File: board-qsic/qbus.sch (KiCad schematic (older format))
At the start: 0 parts

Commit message: Reworked board from template.  Changed schematic to let me use the bus drivers and level converters more efficiently so to get all the signals.
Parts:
- added C501, C502: 100nF, Capacitor_SMD:C_0603_1608Metric, symbol Device:C
- added R501, R502: 4.7k, Resistor_SMD:R_0603_1608Metric, symbol Device:R
- added R503: 2.4k, Resistor_SMD:R_0603_1608Metric, symbol Device:R
- added U101: XC7A75T-CSG324, Package_BGA:BGA-324_15.0x15.0mm_Layout18x18_P0.8mm_Ball0.5mm_Pad0.4mm_NSMD, symbol FPGA_Xilinx_Artix7:XC7A75T-CSG324
- added U501: MT25Q-so8, Package_DFN_QFN:DFN-8-1EP_6x5mm_P1.27mm_EP4x4mm, symbol myLib:MT25Q-mlp8
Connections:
- new net: R503.2, U101.L13 (IO_L6P_T0_FCS_B_14), U501.1 (~S)
- new net: U101.K18 (IO_L1N_T0_D01_DIN_14), U501.2 (DQ1)
- new net: R501.2, U101.L14 (IO_L2P_T0_D02_14), U501.3 (~W~/DQ2)
- new net: U101.K17 (IO_L1P_T0_D00_MOSI_14), U501.5 (DQ0)
- new net: R502.2, U101.M14 (IO_L2N_T0_D03_14), U501.7 (~HOLD~/DQ3)
- new net 3V3: C501.1, C502.1, R501.1, R502.1, R503.1, U101.L17 (VCCO_14), U101.N13 (VCCO_14), U101.P16 (VCCO_14), U101.T12 (VCCO_14), U101.U15 (VCCO_14), U101.V18 (VCCO_14), U501.8 (Vcc)
- new net CCLK: U501.6 (C)
- new net GND: C501.2, C502.2, U501.4 (Vss), U501.9 (EP)

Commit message: Design of prototype is done.  Needs checking before sending out.
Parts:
- added C306, C307: 100nF, Capacitor_SMD:C_0603_1608Metric, symbol Device:C
- added C503, C505, C506, C507: 100nF, Capacitor_SMD:C_0603_1608Metric, symbol Device:C_Small
- added C504: 150uF, Capacitor_SMD:CP_Elec_6.3x5.7, symbol Device:CP1_Small
- added C509, C510: 1uF, Capacitor_SMD:C_0603_1608Metric, symbol Device:C_Small
- added C511: 10nF, Capacitor_SMD:C_0603_1608Metric, symbol Device:C_Small
- added D501, D502, D503, D504, D505, D506, D507, D508: green, LED_SMD:LED_0603_1608Metric, symbol Device:LED_Small_ALT
- added J301, J302: SD Card, Connector_Card:microSD_HC_Hirose_DM3BT-DSF-PEJS, symbol Connector:Micro_SD_Card_Det
- added J501: USB_A, myMods:USB-A-Amphenol-UE27, symbol Connector:USB_A
- added P501: Indicator Panel, myMods:Box_Header_2x05_P2.54mm, symbol Connector_Generic:Conn_02x05_Odd_Even
- added R306, R307, R308, R309, R310, R311, R312, R313, R314, R315: 50k, Resistor_SMD:R_0603_1608Metric, symbol Device:R
- added R504, R505, R506, R507, R508, R509, R510, R511: 240, Resistor_SMD:R_0603_1608Metric, symbol Device:R
- added R512, R513: 100k, Resistor_SMD:R_0603_1608Metric, symbol Device:R
- added R514: 56.2k, Resistor_SMD:R_0603_1608Metric, symbol Device:R
- added R515: 20k, Resistor_SMD:R_0603_1608Metric, symbol Device:R
- added R516: 8.06k, Resistor_SMD:R_0603_1608Metric, symbol Device:R
- added S501: Config, Button_Switch_THT:SW_DIP_SPSTx08_Slide_6.7x21.88mm_W7.62mm_P2.54mm_LowProfile, symbol myLib:DIP-Switch-8
- added unit 2 of U101
- added U502: TPS2561, Package_SON:VSON-10-1EP_3x3mm_P0.5mm_EP1.65x2.4mm_ThermalVias, symbol Interface_USB:TPS2561
- added U503: MAX3033E, Package_SO:TSSOP-16_4.4x5mm_P0.65mm, symbol myLib:MAX3033E
- added U504: USB3340, Package_DFN_QFN:QFN-32-1EP_5x5mm_P0.5mm_EP3.45x3.45mm, symbol myLib:USB3340
- added X501: ASE-24.000MHz, Oscillator:Oscillator_SMD_Abracon_ASE-4Pin_3.2x2.5mm, symbol Oscillator:ASE-xxxMHz
- U501: value MT25Q-so8 -> MT25Q-mlq8
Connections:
- net 3V3: now also U101.A17 (VCCO_15), U101.C13 (VCCO_15), U101.D16 (VCCO_15), U101.G15 (VCCO_15), U101.H18 (VCCO_15), U101.K14 (VCCO_15), C306.1, C307.1, C505.1, C506.1, C507.1, C511.1, J301.4 (VDD), J302.4 (VDD), R306.1, R307.1, R308.1, R309.1, R310.1, R311.1, R312.1, R313.1, R314.1, R315.1, R504.1, R505.1, R506.1, R507.1, R508.1, R509.1, R510.1, R511.1, U101.K4 (VCCO_34), U101.N3 (VCCO_34), U101.P6 (VCCO_34), U101.T2 (VCCO_34), U101.U5 (VCCO_34), U101.V8 (VCCO_34), U503.12 (EN34), U503.16 (VDD), U503.4 (EN12), U504.11 (REFSEL[1]), U504.14 (REFSEL[2]), U504.21 (VBAT), U504.32 (VDDIO), U504.8 (REFSEL[0]), X501.4 (Vdd)
- net 5V0: now also C503.1, R512.1, R513.1, U502.2 (IN), U502.3 (IN)
- net GND: now also C306.2, C307.2, C503.2, C504.2, C505.2, C506.2, C507.2, C509.2, C510.2, C511.2, J301.10 (DET_A), J301.11 (SHIELD), J301.6 (VSS), J302.10 (DET_A), J302.11 (SHIELD), J302.6 (VSS), J501.4 (GND), J501.5 (Shield), P501.3 (Pin_3), P501.8 (Pin_8), R514.2, R516.2, S501.10, S501.11, S501.12, S501.13, S501.14, S501.15, S501.16, S501.9, U502.1 (GND), U502.11 (PAD), U502.4 (EN1), U503.8 (GND), U504.33 (GND), X501.2 (GND)
- net RIRQ6: now reaches U101.A11 (IO_L4N_T0_15)
- net RDAL17: now reaches U101.A13 (IO_L9P_T1_DQS_AD3P_15)
- net RRPLY: now reaches U101.A14 (IO_L9N_T1_DQS_AD3N_15)
- net RDOUT: now reaches U101.A15 (IO_L8P_T1_AD10P_15)
- net TIRQ5: now reaches U101.A16 (IO_L8N_T1_AD10N_15)
- net TDAL17: now reaches U101.A18 (IO_L10N_T1_AD11N_15)
- net RIRQ5: now reaches U101.B12 (IO_L3N_T0_DQS_AD1N_15)
- net RDAL16: now reaches U101.B13 (IO_L2P_T0_AD8P_15)
- net RIRQ4: now reaches U101.B16 (IO_L7P_T1_AD2P_15)
- net TDAL16: now reaches U101.B17 (IO_L7N_T1_AD2N_15)
- net TRPLY: now reaches U101.B18 (IO_L10P_T1_AD11P_15)
- net TIRQ6: now reaches U101.C15 (IO_L12N_T1_MRCC_15)
- net RWTBT: now reaches U101.C16 (IO_L20P_T3_A20_15)
- net TDOUT: now reaches U101.C17 (IO_L20N_T3_A19_15)
- net RSYNC: now reaches U101.D15 (IO_L12P_T1_MRCC_15)
- net TSYNC: now reaches U101.D17 (IO_L16N_T2_A27_15)
- net TDIN: now reaches U101.D18 (IO_L21N_T3_DQS_A18_15)
- net RDIN: now reaches U101.E15 (IO_L11P_T1_SRCC_15)
- net RHALT: now reaches U101.E16 (IO_L11N_T1_SRCC_15)
- net RIAKI: now reaches U101.E17 (IO_L16P_T2_A28_15)
- net RBS7: now reaches U101.E18 (IO_L21P_T3_DQS_15)
- net TWTBT: now reaches U101.F13 (IO_L5P_T0_AD9P_15)
- net TIRQ4: now reaches U101.F14 (IO_L5N_T0_AD9N_15)
- net RDMR: now reaches U101.F16 (IO_L14N_T2_SRCC_15)
- net RREF: now reaches U101.F18 (IO_L22N_T3_A16_15)
- net TDMR: now reaches U101.G14 (IO_L15N_T2_DQS_ADV_B_15)
- net TREF: now reaches U101.G16 (IO_L13N_T2_MRCC_15)
- net TIAKO: now reaches U101.G17 (IO_L18N_T2_A23_15)
- net TBS7: now reaches U101.G18 (IO_L22P_T3_A17_15)
- net RPOK: now reaches U101.H14 (IO_L15P_T2_DQS_15)
- net RDAL0: now reaches U101.H16 (IO_L13P_T2_MRCC_15)
- net TINIT: now reaches U101.H17 (IO_L18P_T2_A24_15)
- net RDAL1: now reaches U101.J13 (IO_L17N_T2_A25_15)
- net TDAL1: now reaches U101.J14 (IO_L19P_T3_A22_15)
- net RDCOK: now reaches U101.J15 (IO_L24N_T3_RS0_15)
- net RINIT: now reaches U101.J17 (IO_L23P_T3_FOE_B_15)
- net RDMGI: now reaches U101.J18 (IO_L23N_T3_FWE_B_15)
- net TDAL0: now reaches U101.K13 (IO_L17P_T2_A26_15)
- net TDAL18: now reaches U101.K15 (IO_L24P_T3_RS1_15)
- net TDMGO: now reaches U101.K16 (IO_25_15)
- net TDAL2: now reaches U101.L18 (IO_L4P_T0_D04_14)
- net TDAL20: now reaches U101.M13 (IO_L6N_T0_D08_VREF_14)
- net TDAL19: now reaches U101.M16 (IO_L10P_T1_D14_14)
- net RDAL5: now reaches U101.M17 (IO_L10N_T1_D15_14)
- net RDAL8: now reaches U101.M18 (IO_L4N_T0_D05_14)
- net RDAL2: now reaches U101.N14 (IO_L8P_T1_D11_14)
- net RDAL18: now reaches U101.N15 (IO_L11P_T1_SRCC_14)
- net TDAL3: now reaches U101.N16 (IO_L11N_T1_SRCC_14)
- net RDAL7: now reaches U101.N17 (IO_L9P_T1_DQS_14)
- net RDAL19: now reaches U101.P14 (IO_L8N_T1_D12_14)
- net RDAL3: now reaches U101.P15 (IO_L13P_T2_MRCC_14)
- net RDAL9: now reaches U101.P17 (IO_L12P_T1_MRCC_14)
- net RSACK: now reaches U101.P18 (IO_L9N_T1_DQS_D13_14)
- net TDAL11: now reaches U101.R10 (IO_25_14)
- net RDAL21: now reaches U101.R13 (IO_L5N_T0_D07_14)
- net RDAL20: now reaches U101.R15 (IO_L13N_T2_MRCC_14)
- net RDAL4: now reaches U101.R16 (IO_L15P_T2_DQS_RDWR_B_14)
- net TDAL21: now reaches U101.R17 (IO_L12N_T1_MRCC_14)
- net TDAL4: now reaches U101.R18 (IO_L7P_T1_D09_14)
- net TDAL15: now reaches U101.T10 (IO_L24N_T3_A00_D16_14)
- net TIRQ7: now reaches U101.T11 (IO_L19P_T3_A10_D26_14)
- net RDAL11: now reaches U101.T13 (IO_L23P_T3_A03_D19_14)
- net REVNT: now reaches U101.T14 (IO_L14P_T2_SRCC_14)
- net TDAL8: now reaches U101.T15 (IO_L14N_T2_SRCC_14)
- net RDAL6: now reaches U101.T16 (IO_L15N_T2_DQS_DOUT_CSO_B_14)
- net TDAL6: now reaches U101.T18 (IO_L7N_T1_D10_14)
- net TDAL13: now reaches U101.U11 (IO_L19N_T3_A09_D25_VREF_14)
- net RDAL14: now reaches U101.U12 (IO_L20P_T3_A08_D24_14)
- net RDAL15: now reaches U101.U13 (IO_L23N_T3_A02_D18_14)
- net RDAL13: now reaches U101.U14 (IO_L22P_T3_A05_D21_14)
- net TDAL9: now reaches U101.U16 (IO_L18P_T2_A12_D28_14)
- net TDAL7: now reaches U101.U17 (IO_L17P_T2_A14_D30_14)
- net TDAL5: now reaches U101.U18 (IO_L17N_T2_A13_D29_14)
- net TDAL14: now reaches U101.V10 (IO_L21P_T3_DQS_14)
- net TDAL12: now reaches U101.V11 (IO_L21N_T3_DQS_A06_D22_14)
- net TDAL10: now reaches U101.V12 (IO_L20N_T3_A07_D23_14)
- net RDAL12: now reaches U101.V14 (IO_L22N_T3_A04_D20_14)
- net RIRQ7: now reaches U101.V15 (IO_L16P_T2_CSI_B_14)
- net RDAL10: now reaches U101.V16 (IO_L16N_T2_A15_D31_14)
- net TSACK: now reaches U101.V17 (IO_L18N_T2_A11_D27_14)
- new net: C504.1, J501.1 (VBUS), R515.2, U502.8 (OUT2)
- new net: J501.2 (D-), U504.19 (DM)
- new net: J501.3 (D+), U504.18 (DP)
- new net: U502.5 (EN2), U504.17 (CPEN)
- new net: C509.1, U504.20 (VDD33), U504.23 (ID)
- new net: R515.1, U504.22 (VBUS)
- new net: R516.1, U504.24 (RBIAS)
- new net: U504.26 (XI/REFCLK), X501.3 (OUT)
- new net: C510.1, U504.28 (VDD18)
- new net: R512.2, U502.10 (~FAULT1)
- new net: R513.2, U502.6 (~FAULT2)
- new net: R514.1, U502.7 (ILM)
- new net: D501.2 (A), R504.2
- new net: D502.2 (A), R505.2
- new net: D503.2 (A), R506.2
- new net: D504.2 (A), R507.2
- new net: D505.2 (A), R508.2
- new net: D506.2 (A), R509.2
- new net: D507.2 (A), R510.2
- new net: D508.2 (A), R511.2
- new net 1V8: U101.B10 (VCCO_16)
- new net IPblank_N: P501.7 (Pin_7), U503.5 (O2-)
- new net IPblank_P: P501.6 (Pin_6), U503.6 (O2+)
- new net IPclk_N: P501.10 (Pin_10), U503.3 (O1-)
- new net IPclk_P: P501.9 (Pin_9), U503.2 (O1+)
- new net IPdata_N: P501.2 (Pin_2), U503.13 (O4-)
- new net IPdata_P: P501.1 (Pin_1), U503.14 (O4+)
- new net IPlatch_N: P501.5 (Pin_5), U503.11 (O3-)
- new net IPlatch_P: P501.4 (Pin_4), U503.10 (O3+)
- new net LED_0: D501.1 (K), U101.K3 (IO_L2P_T0_34)
- new net LED_1: D502.1 (K), U101.K5 (IO_L5P_T0_34)
- new net LED_2: D503.1 (K), U101.K6 (IO_0_34)
- new net LED_3: D504.1 (K), U101.L4 (IO_L5N_T0_34)
- new net LED_4: D505.1 (K), U101.L5 (IO_L6N_T0_VREF_34)
- new net LED_5: D506.1 (K), U101.N5 (IO_L13P_T2_MRCC_34)
- new net LED_6: D507.1 (K), U101.M6 (IO_L18P_T2_34)
- new net LED_7: D508.1 (K), U101.M3 (IO_L4P_T0_34)
- new net SW_0: S501.8, U101.L1 (IO_L1P_T0_34)
- new net SW_1: S501.7, U101.L3 (IO_L2N_T0_34)
- new net SW_2: S501.6, U101.M1 (IO_L1N_T0_34)
- new net SW_3: S501.5, U101.M2 (IO_L4N_T0_34)
- new net SW_4: S501.4, U101.N1 (IO_L3N_T0_DQS_34)
- new net SW_5: S501.3, U101.N2 (IO_L3P_T0_DQS_34)
- new net SW_6: S501.2, U101.P2 (IO_L15P_T2_DQS_34)
- new net SW_7: S501.1, U101.R1 (IO_L17P_T2_34)
- new net ip_blank: U101.M4 (IO_L16P_T2_34), U503.7 (I2)
- new net ip_clk: U101.N4 (IO_L16N_T2_34), U503.1 (I1)
- new net ip_data: U101.R2 (IO_L15N_T2_DQS_34), U503.15 (I4)
- new net ip_latch: U101.P3 (IO_L14N_T2_SRCC_34), U503.9 (I3)
- new net pin11: U101.L6 (IO_L6P_T0_34)
- new net sd0_clk: J301.5 (CLK), U101.T1 (IO_L17N_T2_34)
- new net sd0_cmd: J301.3 (CMD), R308.2, U101.T4 (IO_L12N_T1_MRCC_34)
- new net sd0_dat0: J301.7 (DAT0), R307.2, U101.U1 (IO_L7P_T1_34)
- new net sd0_dat1: J301.8 (DAT1), R306.2, U101.U2 (IO_L9P_T1_DQS_34)
- new net sd0_dat2: J301.1 (DAT2), R310.2, U101.P4 (IO_L14P_T2_SRCC_34)
- new net sd0_dat3: J301.2 (DAT3/CD), R309.2, U101.R3 (IO_L11P_T1_SRCC_34)
- new net sd0_det: J301.9 (DET_B), U101.T3 (IO_L11N_T1_SRCC_34)
- new net sd1_clk: J302.5 (CLK), U101.V1 (IO_L7N_T1_34)
- new net sd1_cmd: J302.3 (CMD), R313.2, U101.R5 (IO_L19N_T3_VREF_34)
- new net sd1_dat0: J302.7 (DAT0), R312.2, U101.R6 (IO_L19P_T3_34)
- new net sd1_dat1: J302.8 (DAT1), R311.2, U101.V4 (IO_L10N_T1_34)
- new net sd1_dat2: J302.1 (DAT2), R315.2, U101.U3 (IO_L8N_T1_34)
- new net sd1_dat3: J302.2 (DAT3/CD), R314.2, U101.U4 (IO_L8P_T1_34)
- new net sd1_det: J302.9 (DET_B), U101.V2 (IO_L9N_T1_DQS_34)
- new net usb0_clk60: U101.T5 (IO_L12P_T1_MRCC_34), U504.1 (CLKOUT)
- new net usb0_d0: U101.V9 (IO_L21N_T3_DQS_34), U504.3 (DATA0)
- new net usb0_d1: U101.T8 (IO_L24N_T3_34), U504.4 (DATA1)
- new net usb0_d2: U101.U8 (IO_25_34), U504.5 (DATA2)
- new net usb0_d3: U101.V7 (IO_L20P_T3_34), U504.6 (DATA3)
- new net usb0_d4: U101.U7 (IO_L22P_T3_34), U504.7 (DATA4)
- new net usb0_d5: U101.V6 (IO_L20N_T3_34), U504.9 (DATA5)
- new net usb0_d6: U101.U6 (IO_L22N_T3_34), U504.10 (DATA6)
- new net usb0_d7: U101.V5 (IO_L10P_T1_34), U504.13 (DATA7)
- new net usb0_dir: U101.R8 (IO_L24P_T3_34), U504.31 (DIR)
- new net usb0_nxt: U101.U9 (IO_L21P_T3_DQS_34), U504.2 (NXT)
- new net usb0_resetb: U101.T6 (IO_L23N_T3_34), U504.27 (RESETB)
- new net usb0_stp: U101.R7 (IO_L23P_T3_34), U504.29 (STP)
- no-connect marks 0 -> 31
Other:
- note added: "Clock Inputs:\nRSYNC\nRDIN (check SRCC)\nREVNT\nusb_clk"
- moved on the sheet: C501, C502, R501, R502, R503, U101A, U501

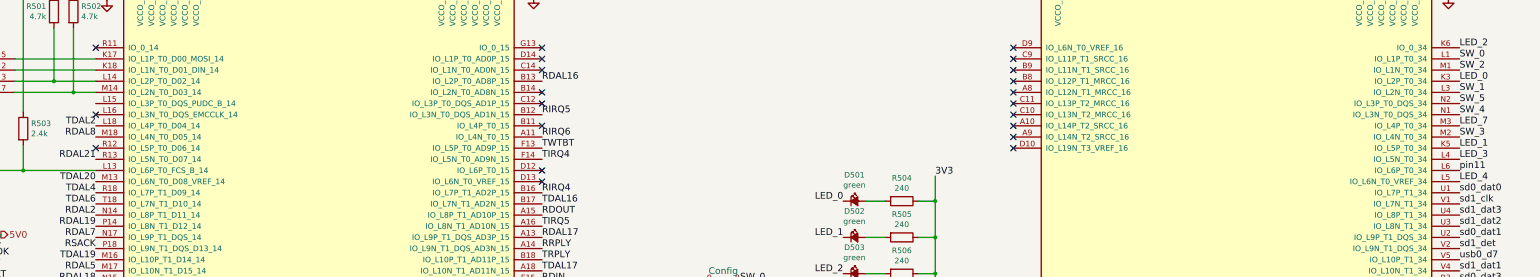
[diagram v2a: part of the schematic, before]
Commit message: A few fixups from ERC.  Ground CS# on the memory chip.
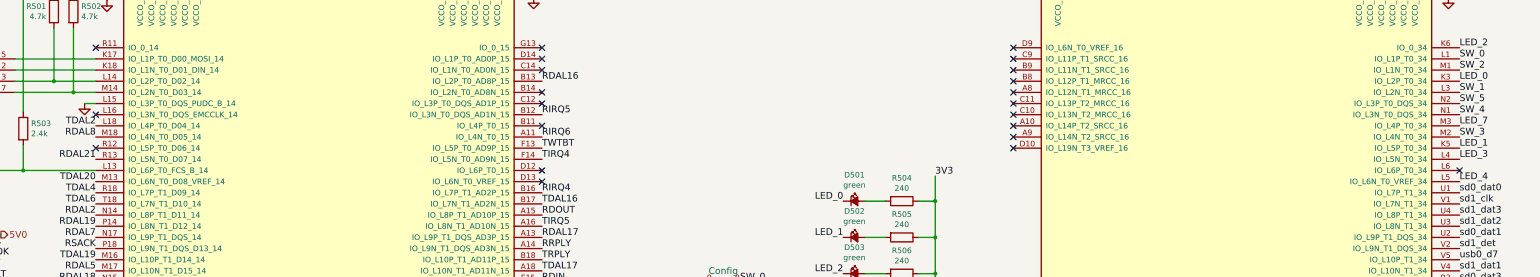
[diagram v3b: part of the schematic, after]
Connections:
- net GND: now also U101.L15 (IO_L3P_T0_DQS_PUDC_B_14)
- net pin11: no longer names the net of U101.L6 (IO_L6P_T0_34)
- no-connect marks 31 -> 32
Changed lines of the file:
@@
 	1    0    0    -1
 $EndComp
-Text Label 15500 2700 0    60   ~ 0
-pin11
 Text Label 9975 2975 2    60   ~ 0
 LED_0
@@
 NoConn ~ 7275 1700
 NoConn ~ 7275 1600
+$Comp
+L power:GND #PWR0151
+U 1 1 5DACEE72
+P 3175 2100
+F 0 "#PWR0151" H 3175 1850 50  0001 C CNN
+F 1 "GND" H 3180 1927 50  0001 C CNN
+F 2 "" H 3175 2100 50  0001 C CNN
+F 3 "" H 3175 2100 50  0001 C CNN
+	1    3175 2100
+	1    0    0    -1
+$EndComp
+Wire Wire Line
+	3275 2100 3175 2100
+NoConn ~ 15500 2700
 $EndSCHEMATC

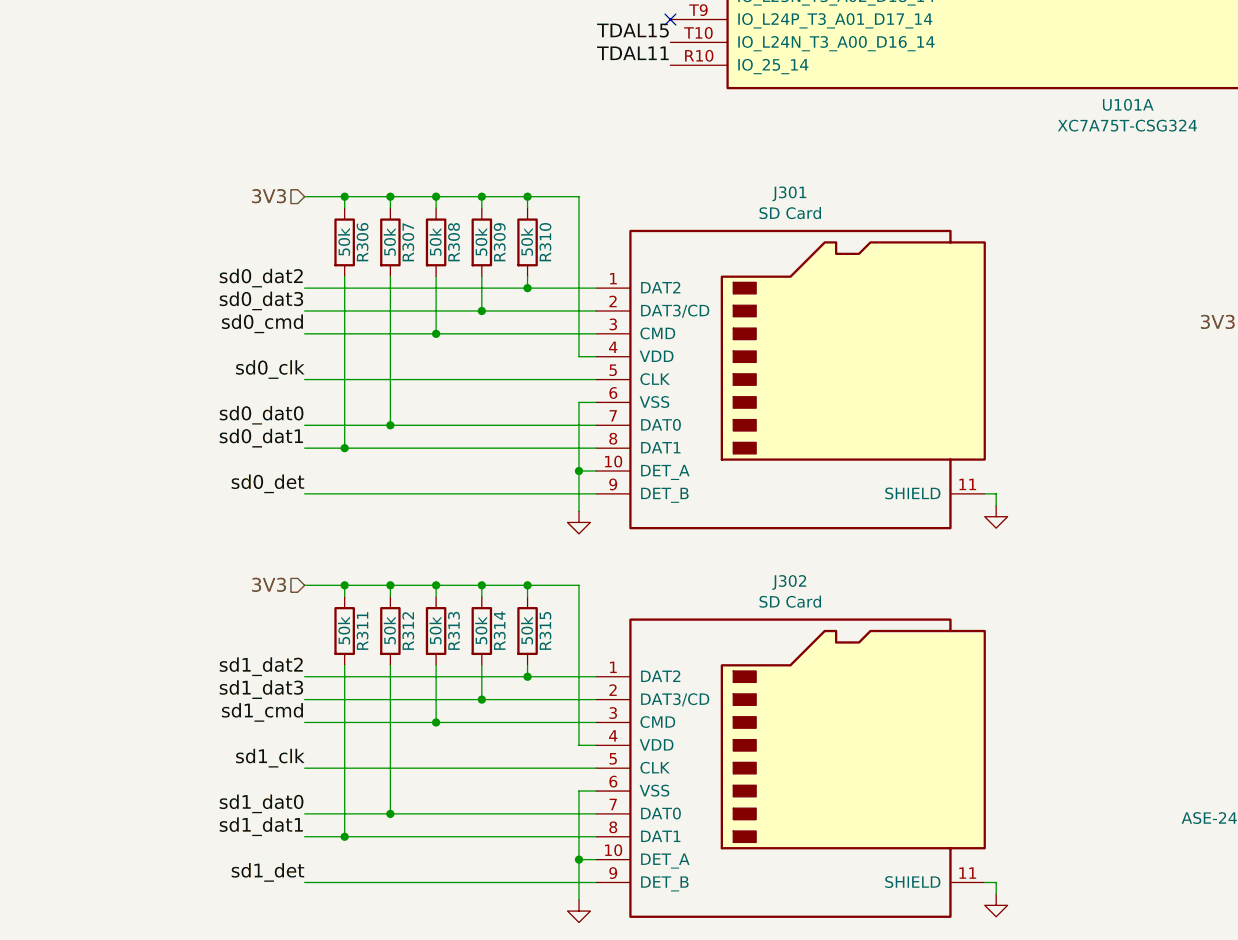
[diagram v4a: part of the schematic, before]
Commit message: Add small resistor and large capacitor to SD card power.
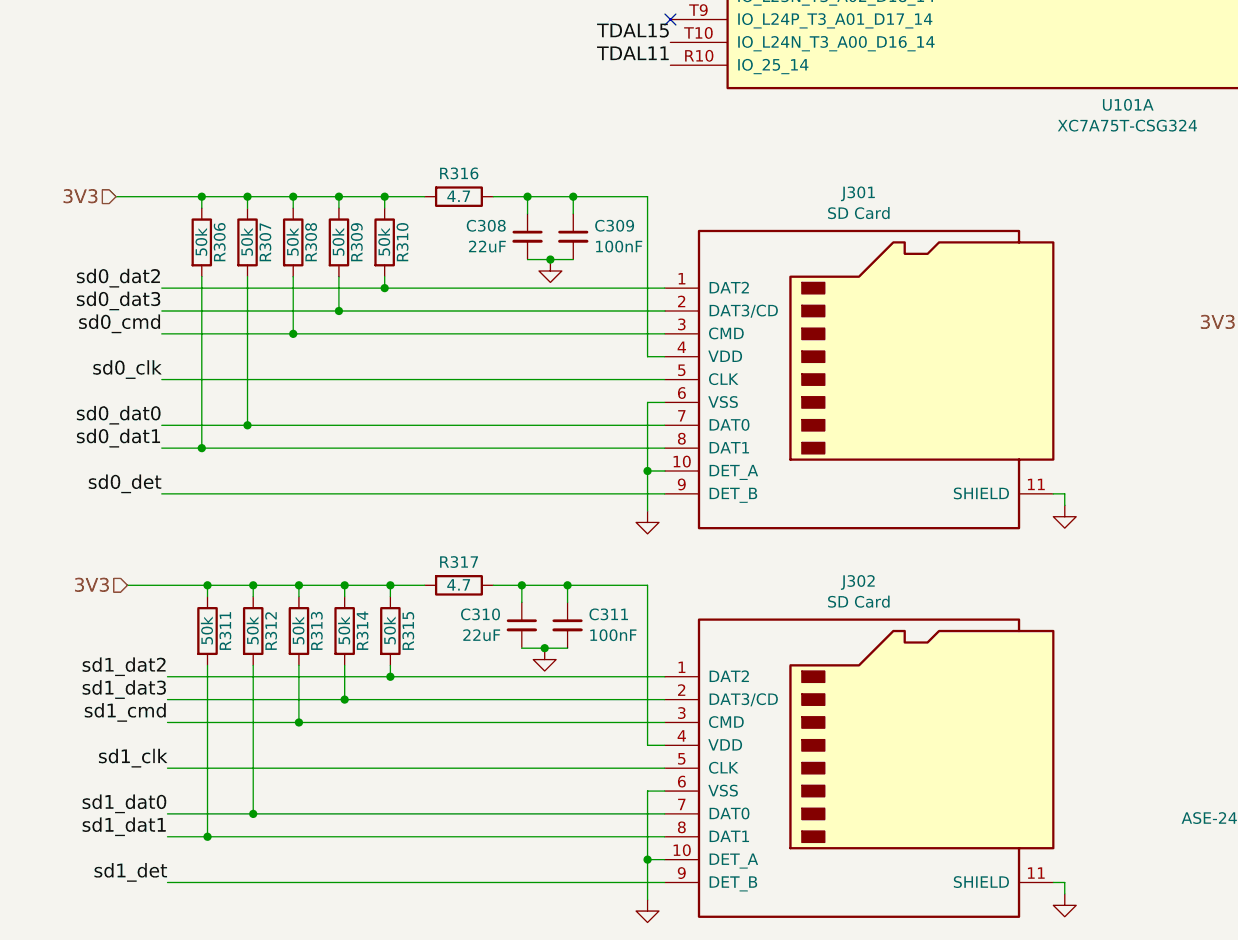
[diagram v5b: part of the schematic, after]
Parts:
- added C308, C310: 22uF, Capacitor_SMD:C_0805_2012Metric, symbol Device:C_Small
- added C309, C311: 100nF, Capacitor_SMD:C_0603_1608Metric, symbol Device:C_Small
- added R316, R317: 4.7, Resistor_SMD:R_0603_1608Metric, symbol Device:R
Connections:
- net 3V3: now also R316.2, R317.2; no longer J301.4 (VDD), J302.4 (VDD)
- net GND: now also C308.2, C309.2, C310.2, C311.2
- new net: C308.1, C309.1, J301.4 (VDD), R316.1
- new net: C310.1, C311.1, J302.4 (VDD), R317.1
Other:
- moved on the sheet: J301, J302, R306, R307, R308, R309, R310, R311, R312, R313, R314, R315

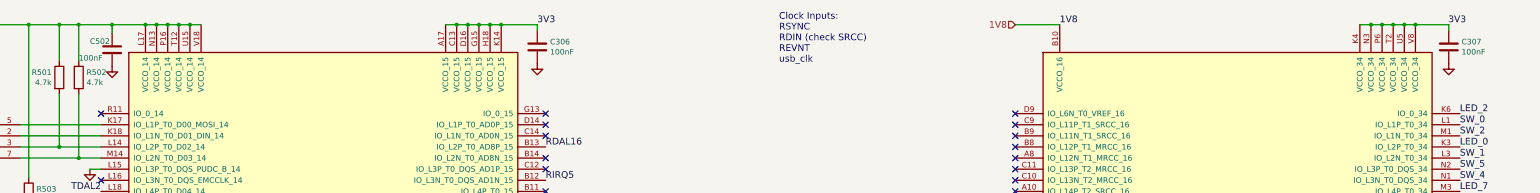
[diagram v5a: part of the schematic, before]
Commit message: Changed some capacitors from 100nF to 10uF
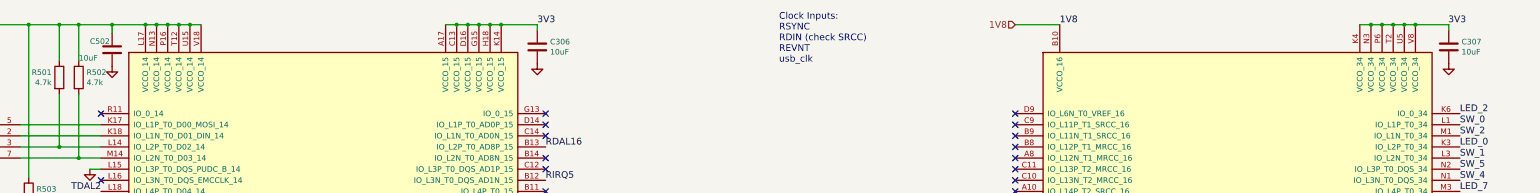
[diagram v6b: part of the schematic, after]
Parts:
- C306, C307, C502: value 100nF -> 10uF
- R316, R317: manf# RC0603FR-0749K9L -> (none)
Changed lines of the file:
@@
 EESchema Schematic File Version 4
-LIBS:qsic-cache
 EELAYER 30 0
 EELAYER END
@@
 P 3375 1025
 F 0 "C502" H 3175 1100 50  0000 L CNN
-F 1 "100nF" H 3075 950 50  0000 L CNN
+F 1 "10uF" H 3075 950 50  0000 L CNN
 F 2 "Capacitor_SMD:C_0603_1608Metric" H 3413 875 50  0001 C CNN
 F 3 "~" H 3375 1025 50  0001 C CNN
@@
 P 7200 1000
 F 0 "C306" H 7315 1046 50  0000 L CNN
-F 1 "100nF" H 7315 955 50  0000 L CNN
+F 1 "10uF" H 7315 955 50  0000 L CNN
 F 2 "Capacitor_SMD:C_0603_1608Metric" H 7238 850 50  0001 C CNN
 F 3 "~" H 7200 1000 50  0001 C CNN
@@
 P 15400 1000
 F 0 "C307" H 15515 1046 50  0000 L CNN
-F 1 "100nF" H 15515 955 50  0000 L CNN
+F 1 "10uF" H 15515 955 50  0000 L CNN
 F 2 "Capacitor_SMD:C_0603_1608Metric" H 15438 850 50  0001 C CNN
 F 3 "~" H 15400 1000 50  0001 C CNN
@@
 F 2 "Resistor_SMD:R_0603_1608Metric" V 2280 8775 50  0001 C CNN
 F 3 "" H 2350 8775 50  0000 C CNN
-F 4 "RC0603FR-0749K9L" H 2350 8775 50  0001 C CNN "manf#"
+F 4 "" H 2350 8775 50  0001 C CNN "manf#"
 	1    2350 8775
 	0    1    1    0
@@
 F 2 "Resistor_SMD:R_0603_1608Metric" V 2280 7075 50  0001 C CNN
 F 3 "" H 2350 7075 50  0000 C CNN
-F 4 "RC0603FR-0749K9L" H 2350 7075 50  0001 C CNN "manf#"
+F 4 "" H 2350 7075 50  0001 C CNN "manf#"
 	1    2350 7075
 	0    1    1    0
